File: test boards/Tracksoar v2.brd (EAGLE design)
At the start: 50.4 x 19.5 mm, 39 parts, among them IC1 BME280, IC2 74AHC1G125DBV, Y1 16MHZ

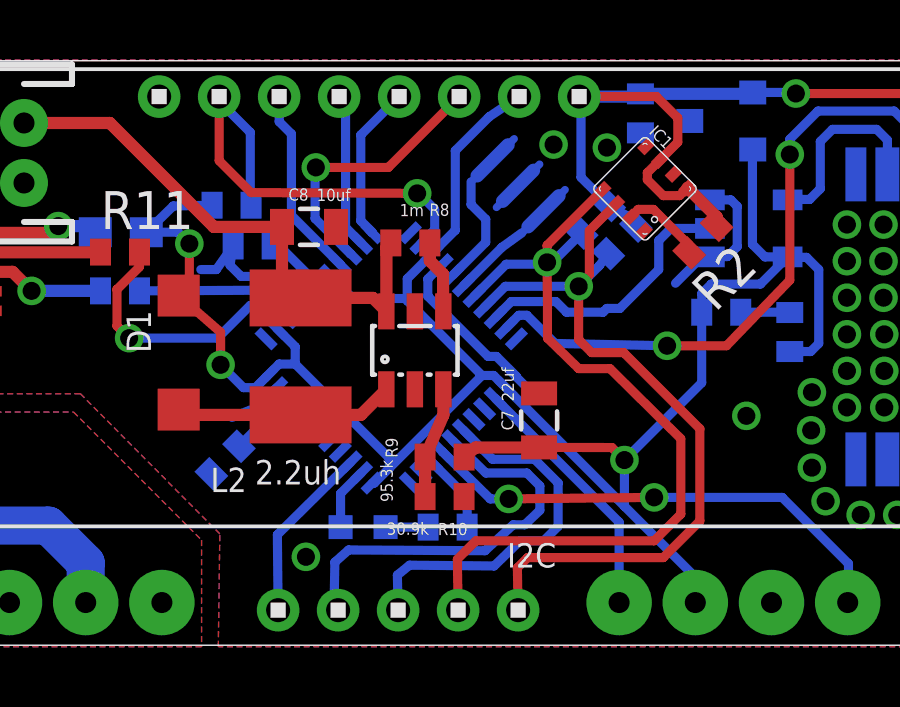
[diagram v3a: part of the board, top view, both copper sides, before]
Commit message: tracksoar v2 rev4
fixed routing issues on ground, cleaned up schematic to remove overlaps
and moved items to their proper area of the schematic.
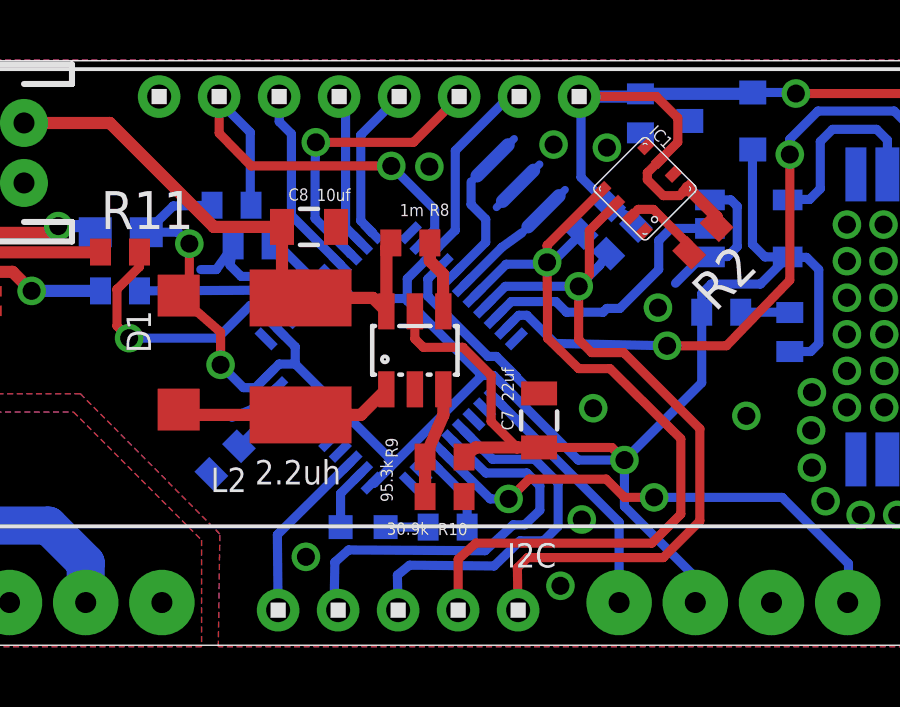
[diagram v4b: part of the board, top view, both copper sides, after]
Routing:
- net VCC: track 75.6 -> 81.8 mm
- net D3: track 16.4 -> 16.9 mm
- net !RESET: track 15.4 -> 14.9 mm
- net GND: vias 66 -> 71
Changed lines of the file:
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@@
 <via x="37.6428" y="4.4704" extent="1-16" drill="0.6"/>
 <via x="38.862" y="4.445" extent="1-16" drill="0.6"/>
+<via x="23.9776" y="2.0574" extent="1-16" drill="0.6"/>
+<via x="19.6088" y="16.0274" extent="1-16" drill="0.6"/>
+<via x="25.0698" y="7.9756" extent="1-16" drill="0.6"/>
+<via x="27.2288" y="11.3284" extent="1-16" drill="0.6"/>
+<via x="24.6888" y="4.2672" extent="1-16" drill="0.6"/>
 <wire x1="2.0066" y1="8.5222" x2="2.4384" y2="6.604" width="0" layer="19" extent="1-1"/>
-<wire x1="22.51073125" y1="9.03606875" x2="23.2664" y2="8.4692" width="0" layer="19" extent="1-16"/>
-<wire x1="27.75159375" y1="15.785771875" x2="26.832353125" y2="16.7050125" width="0" layer="19" extent="1-1"/>
 </signal>
 <signal name="VCC">
@@
 <contactref element="C7" pad="1"/>
 <contactref element="U$4" pad="14"/>
-<contactref element="U$4" pad="34"/>
-<contactref element="U$4" pad="24"/>
 <contactref element="U$4" pad="44"/>
 <contactref element="F1" pad="2"/>
 <contactref element="FTDI" pad="2"/>
-<wire x1="22.157178125" y1="8.66205" x2="21.751428125" y2="9.0678" width="0.3048" layer="16"/>
 <wire x1="21.751428125" y1="9.0678" x2="21.3614" y2="9.0678" width="0.3048" layer="16"/>
 <wire x1="21.3614" y1="9.0678" x2="18.2753" y2="5.9817" width="0.3048" layer="16"/>
 <wire x1="18.2753" y1="5.9817" x2="17.77366875" y2="5.48006875" width="0.3048" layer="16"/>
-<wire x1="17.77366875" y1="5.48006875" x2="17.70240625" y2="5.48006875" width="0.3048" layer="16"/>
 <wire x1="14.166871875" y1="9.015603125" x2="14.60006875" y2="9.4488" width="0.3048" layer="16"/>
 <wire x1="14.60006875" y1="9.4488" x2="15.1384" y2="9.4488" width="0.3048" layer="16"/>
@@
 <wire x1="19.682303125" y1="13.116821875" x2="20.4724" y2="13.90691875" width="0.3048" layer="16"/>
 <wire x1="20.4724" y1="13.90691875" x2="20.4724" y2="16.5608" width="0.3048" layer="16"/>
-<wire x1="20.4724" y1="16.5608" x2="21.6022" y2="17.6906" width="0.3048" layer="16"/>
-<wire x1="21.6022" y1="17.6906" x2="22.6022" y2="18.3642" width="0.3048" layer="16"/>
+<wire x1="20.4724" y1="16.5608" x2="22.288" y2="18.3764" width="0.3048" layer="16"/>
+<wire x1="22.288" y1="18.3764" x2="22.6022" y2="18.3642" width="0.3048" layer="16"/>
 <wire x1="10.1718" y1="13.843" x2="11.071321875" y2="14.717121875" width="0.3048" layer="16"/>
 <wire x1="11.071321875" y1="14.717121875" x2="12.365325" y2="14.742521875" width="0.3048" layer="16"/>
-<wire x1="22.157178125" y1="8.66205" x2="26.1112" y2="4.708028125" width="0.3048" layer="16"/>
 <wire x1="26.1112" y1="4.708028125" x2="28.4734" y2="2.345828125" width="0.3048" layer="16"/>
 <wire x1="28.4734" y1="2.345828125" x2="28.4734" y2="1.4986" width="0.3048" layer="16"/>
@@
 <wire x1="29.0068" y1="12.1158" x2="30.6472" y2="12.1158" width="0.3048" layer="16"/>
 <wire x1="30.6472" y1="12.1158" x2="31.5514" y2="13.02" width="0.3048" layer="16"/>
-<wire x1="23.2664" y1="6.6692" x2="21.1478" y2="6.6658" width="0.4064" layer="1"/>
+<wire x1="23.2664" y1="6.6692" x2="22.530634375" y2="6.66801875" width="0.4064" layer="1"/>
+<wire x1="22.530634375" y1="6.66801875" x2="21.1478" y2="6.6658" width="0.4064" layer="1"/>
 <wire x1="21.1478" y1="6.6658" x2="20.7668" y2="6.35" width="0.4064" layer="1"/>
 <wire x1="23.2664" y1="6.6692" x2="25.6938" y2="6.6658" width="0.3048" layer="1"/>
@@
 <wire x1="14.520425" y1="10.641946875" x2="15.1384" y2="10.023971875" width="0.3048" layer="16"/>
 <wire x1="15.1384" y1="10.023971875" x2="15.1384" y2="9.4488" width="0.3048" layer="16"/>
-<wire x1="18.8722" y1="11.557" x2="19.1262" y2="11.206" width="0" layer="19" extent="1-16"/>
+<contactref element="U$4" pad="24"/>
+<wire x1="21.751428125" y1="9.0678" x2="22.157178125" y2="8.66205" width="0.3048" layer="16"/>
+<wire x1="22.157178125" y1="8.66205" x2="24.570828125" y2="6.2484" width="0.3048" layer="16"/>
+<wire x1="24.570828125" y1="6.2484" x2="26.1112" y2="6.2484" width="0.3048" layer="16"/>
+<wire x1="19.1262" y1="11.206" x2="19.1262" y2="10.287" width="0.3048" layer="1"/>
+<wire x1="19.1262" y1="10.287" x2="19.4056" y2="10.0076" width="0.3048" layer="1"/>
+<wire x1="19.4056" y1="10.0076" x2="20.7264" y2="10.0076" width="0.3048" layer="1"/>
+<wire x1="20.7264" y1="10.0076" x2="21.6662" y2="9.0678" width="0.3048" layer="1"/>
+<wire x1="21.6662" y1="9.0678" x2="21.6662" y2="7.532453125" width="0.3048" layer="1"/>
+<wire x1="21.6662" y1="7.532453125" x2="22.530634375" y2="6.66801875" width="0.3048" layer="1"/>
+<contactref element="U$4" pad="34"/>
+<wire x1="17.70240625" y1="5.48006875" x2="17.77366875" y2="5.48006875" width="0.3048" layer="16"/>
 </signal>
 <signal name="D3">
@@
 <wire x1="21.6408" y1="4.953" x2="22.2504" y2="4.953" width="0.3048" layer="16"/>
 <via x="22.2504" y="4.953" extent="1-16" drill="0.6"/>
-<wire x1="22.2504" y1="4.953" x2="27.1018" y2="5.0038" width="0.3048" layer="1"/>
 <via x="27.1018" y="5.0038" extent="1-16" drill="0.6"/>
 <wire x1="27.1018" y1="5.0038" x2="31.369" y2="5.0038" width="0.3048" layer="16"/>
@@
 <wire x1="33.5788" y1="2.794" x2="33.5788" y2="1.524" width="0.3048" layer="16"/>
 <wire x1="33.5788" y1="1.524" x2="33.5534" y2="1.4986" width="0.3048" layer="16"/>
+<wire x1="22.2504" y1="4.953" x2="22.2758" y2="4.953" width="0.3048" layer="1"/>
+<wire x1="22.2758" y1="4.953" x2="22.9362" y2="5.6134" width="0.3048" layer="1"/>
+<wire x1="22.9362" y1="5.6134" x2="25.5016" y2="5.6134" width="0.3048" layer="1"/>
+<wire x1="25.5016" y1="5.6134" x2="26.1112" y2="5.0038" width="0.3048" layer="1"/>
+<wire x1="26.1112" y1="5.0038" x2="27.1018" y2="5.0038" width="0.3048" layer="1"/>
 </signal>
 <signal name="D4">
@@
 <wire x1="16.982178125" y1="13.116821875" x2="15.7988" y2="14.3002" width="0.3048" layer="16"/>
 <wire x1="15.7988" y1="14.3002" x2="15.7988" y2="16.002" width="0.3048" layer="16"/>
-<wire x1="15.7988" y1="16.002" x2="15.8242" y2="16.002" width="0.3048" layer="16"/>
-<via x="15.8242" y="16.002" extent="1-16" drill="0.6"/>
-<wire x1="15.8242" y1="16.002" x2="18.24" y2="16.002" width="0.3048" layer="1"/>
-<wire x1="18.24" y1="16.002" x2="20.6022" y2="18.3642" width="0.3048" layer="1"/>
+<wire x1="15.7988" y1="16.002" x2="15.8242" y2="16.8402" width="0.3048" layer="16"/>
+<via x="15.8242" y="16.8402" extent="1-16" drill="0.6"/>
+<wire x1="15.8242" y1="16.8402" x2="19.0782" y2="16.8402" width="0.3048" layer="1"/>
+<wire x1="19.0782" y1="16.8402" x2="20.6022" y2="18.3642" width="0.3048" layer="1"/>
 </signal>
 <signal name="SS">
@@
 <wire x1="23.848178125" y1="12.976978125" x2="24.68638125" y2="13.815178125" width="0.3048" layer="16"/>
 <contactref element="U$3" pad="4"/>
-<wire x1="20.5674" y1="1.2446" x2="20.542" y2="2.9398" width="0.3048" layer="1"/>
-<wire x1="20.542" y1="2.9398" x2="21.1582" y2="3.556" width="0.3048" layer="1"/>
-<wire x1="21.1582" y1="3.556" x2="27.1018" y2="3.556" width="0.3048" layer="1"/>
-<wire x1="27.1018" y1="3.556" x2="27.9908" y2="4.445" width="0.3048" layer="1"/>
+<wire x1="20.5674" y1="1.2446" x2="20.5674" y2="2.9398" width="0.3048" layer="1"/>
+<wire x1="20.5674" y1="2.9398" x2="21.1582" y2="3.4798" width="0.3048" layer="1"/>
+<wire x1="21.1582" y1="3.4798" x2="27.0256" y2="3.4798" width="0.3048" layer="1"/>
+<wire x1="27.0256" y1="3.4798" x2="27.9908" y2="4.445" width="0.3048" layer="1"/>
 <wire x1="27.9908" y1="4.445" x2="27.9908" y2="6.9596" width="0.3048" layer="1"/>
 <wire x1="27.9908" y1="6.9596" x2="25.6286" y2="9.2964" width="0.3048" layer="1"/>
@@
 <contactref element="U$4" pad="13"/>
 <wire x1="19.32875" y1="13.470375" x2="19.7866" y2="13.928225" width="0.3048" layer="16"/>
-<via x="19.2024" y="15.1384" extent="1-16" drill="0.6"/>
-<wire x1="19.2024" y1="15.1384" x2="13.665325" y2="15.1638" width="0.3048" layer="1"/>
-<wire x1="13.665325" y1="15.1638" x2="12.6022" y2="16.226925" width="0.3048" layer="1"/>
-<wire x1="12.6022" y1="16.226925" x2="12.6022" y2="18.3642" width="0.3048" layer="1"/>
+<via x="18.3388" y="16.0528" extent="1-16" drill="0.6"/>
+<wire x1="18.3388" y1="16.0528" x2="13.665325" y2="16.0528" width="0.3048" layer="1"/>
+<wire x1="13.665325" y1="16.0528" x2="12.6022" y2="17.141325" width="0.3048" layer="1"/>
+<wire x1="12.6022" y1="17.141325" x2="12.6022" y2="18.3642" width="0.3048" layer="1"/>
 <wire x1="13.665325" y1="14.742521875" x2="13.6398" y2="14.742646875" width="0.3048" layer="16"/>
 <wire x1="13.6398" y1="14.742646875" x2="13.6398" y2="17.1704" width="0.3048" layer="16"/>
 <wire x1="13.6398" y1="17.1704" x2="12.6022" y2="18.208" width="0.3048" layer="16"/>
 <wire x1="12.6022" y1="18.208" x2="12.6022" y2="18.3642" width="0.3048" layer="16"/>
-<wire x1="19.2024" y1="15.1384" x2="19.2532" y2="15.1384" width="0.3048" layer="16"/>
-<wire x1="19.2532" y1="15.1384" x2="19.7866" y2="14.605" width="0.3048" layer="16"/>
+<wire x1="18.3388" y1="16.0528" x2="19.7866" y2="14.605" width="0.3048" layer="16"/>
 <wire x1="19.7866" y1="14.605" x2="19.7866" y2="13.928225" width="0.3048" layer="16"/>
 </signal>

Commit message: tracksoar v2 rev5
added ferrite to 5v output on boost converter. Added 4.7k resistor
between Vin and AREF to provide battery voltage monitoring.
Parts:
- removed C6: 22uf, rcl:C0402
- added L1: BLM15HB121SN1, inductors:0402
- added R12: 4.7k, adafruit:R0402
- moved R5 0.74 mm to (13.0, 15.5)
- moved C5 0.31 mm to (13.4, 13.4)
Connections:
- new net N$19: C7.1, D1.C, L1.1, LT3426.5, R9.2
- net 15V: now also R12.1
- net GND: no longer C6.1
- net N$17: now also R12.2; no longer C6.2
- net VCC: now also L1.2; no longer C7.1, D1.C, LT3426.5, R9.2
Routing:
- net N$19: track 0.00 -> 18.8 mm
- net 15V: track 18.0 -> 35.4 mm
- net VCC: track 81.8 -> 68.5 mm, vias 3 -> 2
- net N$17: track 2.28 -> 4.22 mm
- net GND: track 21.0 -> 20.0 mm, vias 71 -> 73
- net !RESET: track 14.9 -> 14.1 mm
